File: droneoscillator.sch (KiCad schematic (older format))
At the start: 44 parts, among them J1 Conn_01x02, J2 Conn_01x03, Q1 BC337, Q2 BC337, Q3 BC337, Q4 BC337, U1 NE5532

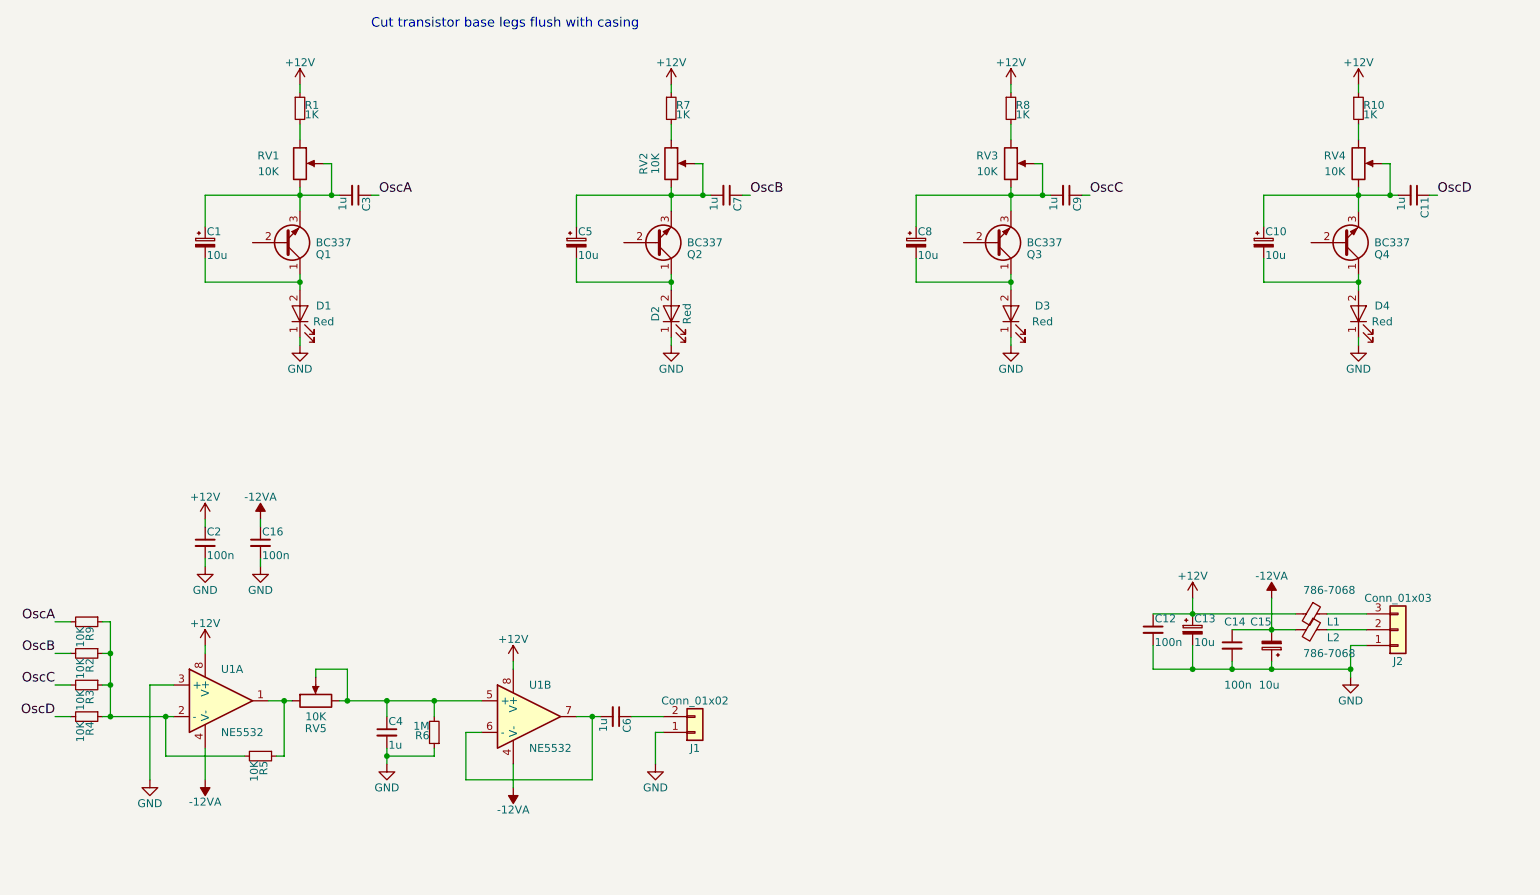
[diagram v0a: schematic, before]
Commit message: Bug fixes after first prototype build
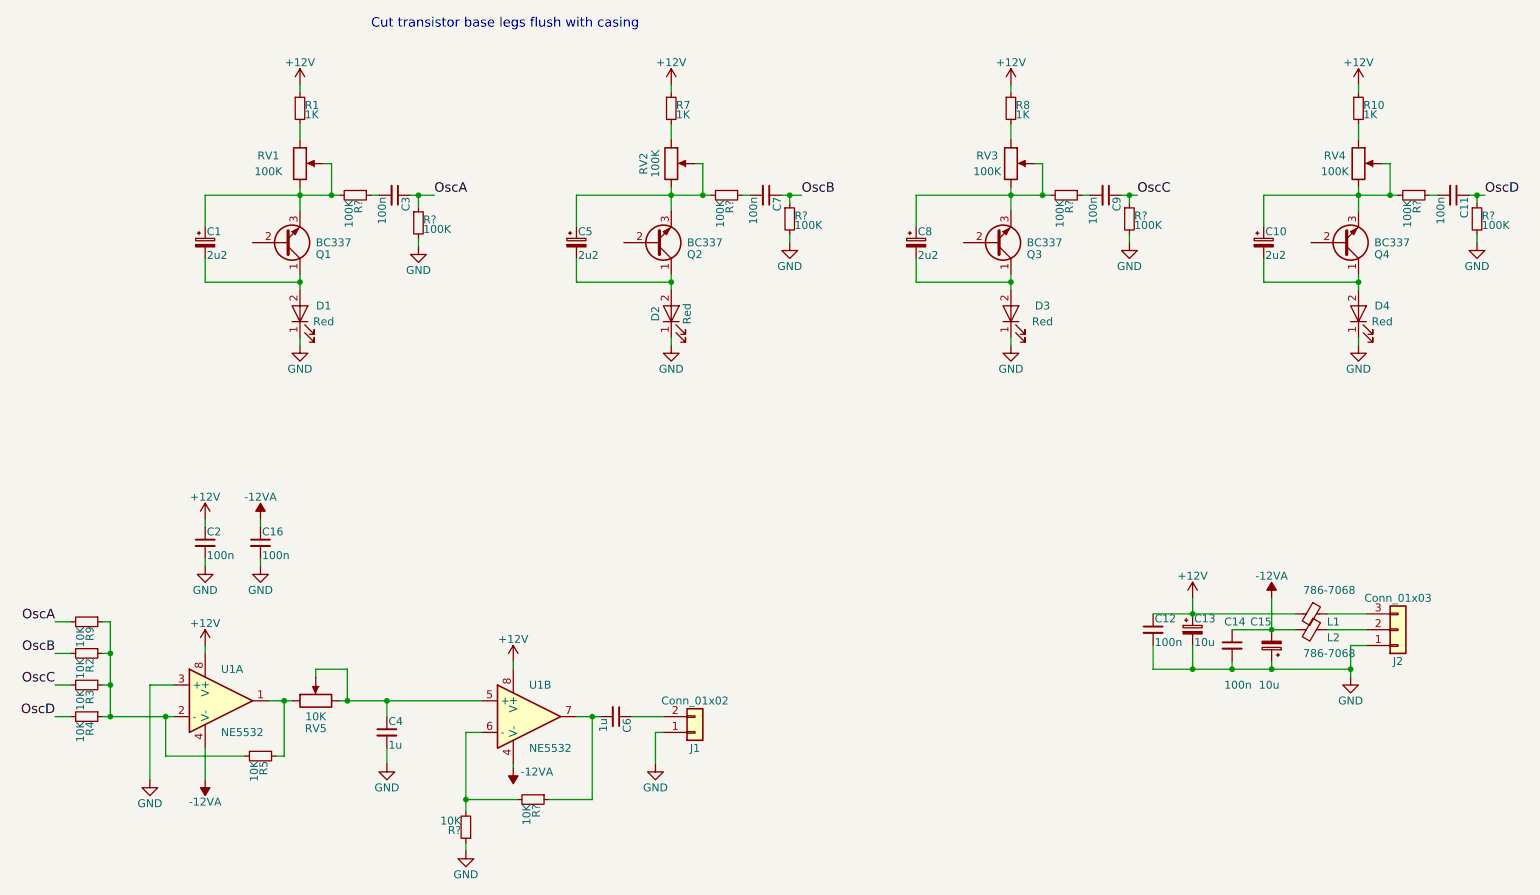
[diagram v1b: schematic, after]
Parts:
- removed R6: 1M, Resistors_THT:R_Axial_DIN0204_L3.6mm_D1.6mm_P7.62mm_Horizontal, symbol droneoscillator-rescue:R_Small
- added R? (x8): 100K, Resistors_THT:R_Axial_DIN0204_L3.6mm_D1.6mm_P7.62mm_Horizontal, symbol droneoscillator-rescue:R_Small
- added R? (x2): 10K, Resistors_THT:R_Axial_DIN0204_L3.6mm_D1.6mm_P7.62mm_Horizontal, symbol droneoscillator-rescue:R_Small
- C1, C10, C5, C8: value 10u -> 2u2
- C11, C3, C7, C9: value 1u -> 100n
- RV1, RV2, RV3, RV4: value 10K -> 100K
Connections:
- net GND: now also R?.1, R?.2, R?.2, R?.2, R?.2
- net OscA: now also R?.1
- net OscB: now also R?.1
- net OscC: now also R?.1
- net OscD: now also R?.1
- net at C1.1, Q1.3 (E), RV1.2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: now also R?.2; no longer C3.2
- net at C5.1, Q2.3 (E), RV2.2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: now also R?.2; no longer C7.2
- net at C8.1, Q3.3 (E), RV3.2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: now also R?.2; no longer C9.2
- net at C10.1, Q4.3 (E), RV4.2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: now also R?.2; no longer C11.2
- net at C6.2, U1.7: now also R?.1; no longer U1.6 (-)
- new net: R?.2, R?.2, U1.6 (-)
- new net: C3.2, R?.1
- new net: C7.2, R?.1
- new net: C9.2, R?.1
- new net: C11.2, R?.1
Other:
- moved on the sheet: C11, C3, C7, C9

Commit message: update after prototype build, new PCB layout
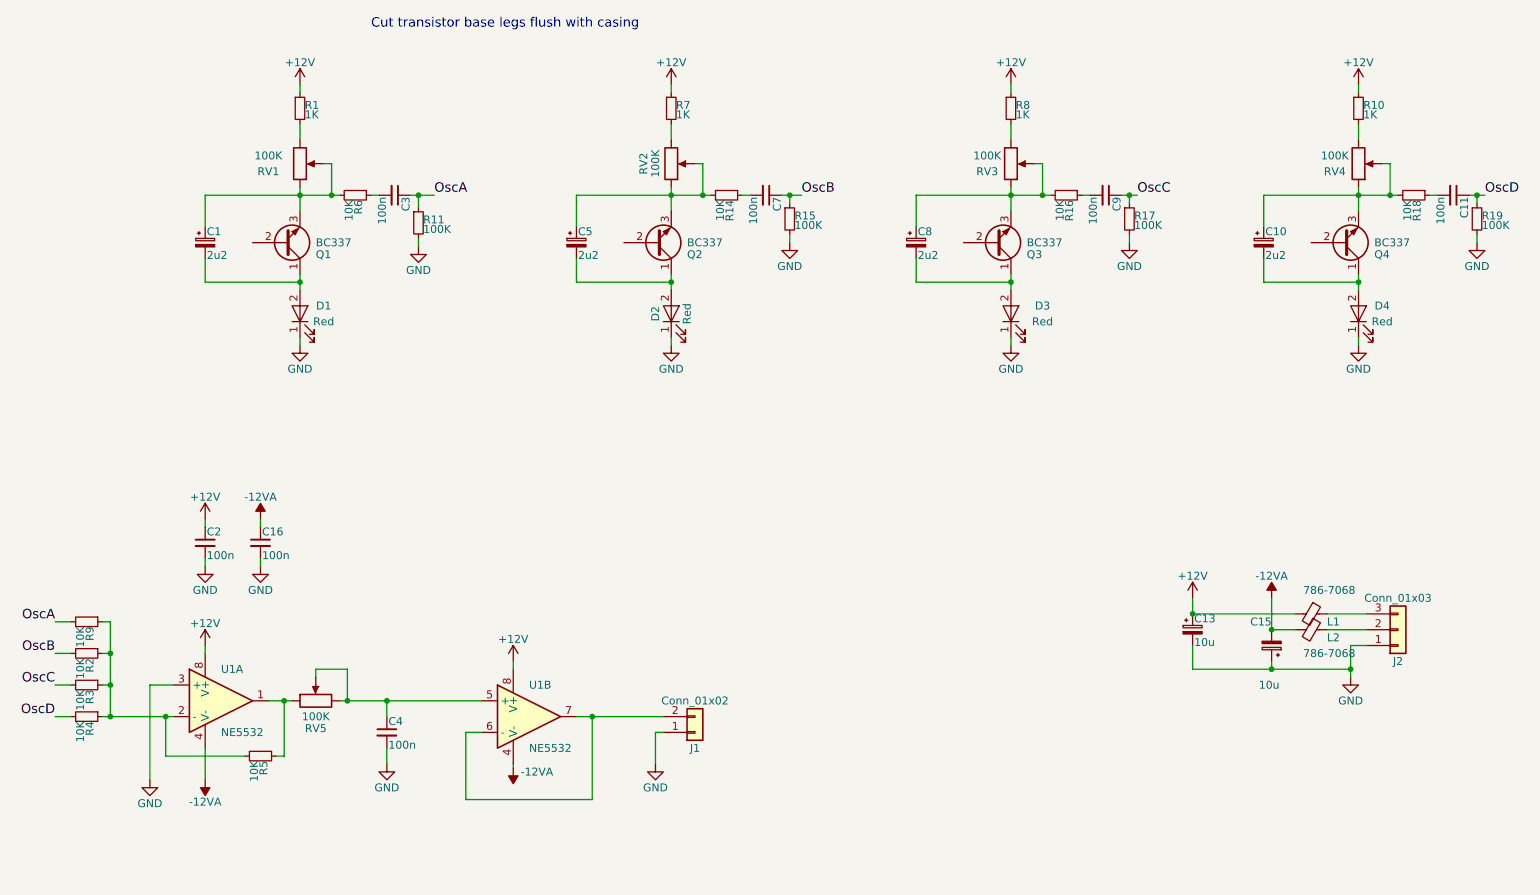
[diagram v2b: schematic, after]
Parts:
- removed C12, C14: 100n, Capacitors_THT:C_Disc_D4.3mm_W1.9mm_P5.00mm, symbol droneoscillator-rescue:C_Small
- removed C6: 1u, Capacitors_THT:C_Disc_D4.3mm_W1.9mm_P5.00mm, symbol droneoscillator-rescue:C_Small
- removed R? (x2): 10K, Resistors_THT:R_Axial_DIN0204_L3.6mm_D1.6mm_P7.62mm_Horizontal, symbol droneoscillator-rescue:R_Small
- C1, C10, C13, C15, C5, C8: footprint Capacitors_THT:CP_Radial_D5.0mm_P2.50mm -> Capacitor_THT:CP_Radial_D4.0mm_P2.00mm
- C11, C16, C2, C3, C7, C9: footprint Capacitors_THT:C_Disc_D4.3mm_W1.9mm_P5.00mm -> Capacitor_THT:C_Disc_D4.3mm_W1.9mm_P5.00mm
- C4: value 1u -> 100n; footprint Capacitors_THT:C_Disc_D4.3mm_W1.9mm_P5.00mm -> Capacitor_THT:C_Disc_D4.3mm_W1.9mm_P5.00mm
- J1: footprint Connectors_JST:JST_XH_B02B-XH-A_02x2.50mm_Straight -> Connector_JST:JST_XH_B02B-XH-A_1x02_P2.50mm_Vertical
- J2: footprint Connectors_JST:JST_XH_B03B-XH-A_03x2.50mm_Straight -> Connector_JST:JST_XH_B03B-XH-A_1x03_P2.50mm_Vertical
- L1, L2: footprint Inductors_SMD:L_0805_HandSoldering -> Inductor_SMD:L_0805_2012Metric
- Q1, Q2, Q3, Q4: footprint TO_SOT_Packages_THT:TO-92_Inline_Wide -> Package_TO_SOT_THT:TO-92_Inline_Wide
- R1, R10, R2, R3, R4, R5, R7, R8, R9: footprint Resistors_THT:R_Axial_DIN0204_L3.6mm_D1.6mm_P7.62mm_Horizontal -> Resistor_THT:R_Axial_DIN0204_L3.6mm_D1.6mm_P7.62mm_Horizontal
- R11, R15, R17, R19: renamed from R?; footprint Resistors_THT:R_Axial_DIN0204_L3.6mm_D1.6mm_P7.62mm_Horizontal -> Resistor_THT:R_Axial_DIN0204_L3.6mm_D1.6mm_P7.62mm_Horizontal
- R14, R16, R18, R6: renamed from R?; value 100K -> 10K; footprint Resistors_THT:R_Axial_DIN0204_L3.6mm_D1.6mm_P7.62mm_Horizontal -> Resistor_THT:R_Axial_DIN0204_L3.6mm_D1.6mm_P7.62mm_Horizontal
- RV5: value 10K -> 100K
- U1: footprint Housings_DIP:DIP-8_W7.62mm_LongPads -> Package_DIP:DIP-8_W7.62mm_Socket_LongPads
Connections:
- net at C1.1, Q1.3 (E), R6.2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: now also RV1.1; no longer RV1.3
- net at R1.2: now also RV1.3; no longer RV1.1
- net at C5.1, Q2.3 (E), R14.2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: now also RV2.1; no longer RV2.3
- net at R7.2: now also RV2.3; no longer RV2.1
- net at RV3.1: now also C8.1, Q3.3 (E), R16.2, RV3.2; no longer R8.2
- net at RV4.1: now also C10.1, Q4.3 (E), R18.2, RV4.2; no longer R10.2
- net at U1.6 (-): now also J1.2 (Pin_2), U1.7
- new net: R8.2, RV3.3
- new net: R10.2, RV4.3

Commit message: schematic bugfix, minor changes to PCB
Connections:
- net at R5.1, U1.1: now also RV5.3; no longer RV5.1
- net at C4.1, RV5.2, U1.5 (+): now also RV5.1; no longer RV5.3
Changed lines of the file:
@@
 F 3 "" H 2850 5150 50  0001 C CNN
 	1    2850 5150
-	0    -1   -1   0
+	0    1    -1   0
 $EndComp
 $Comp

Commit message: silkscreen bugfix
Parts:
- D1, D2, D3, D4: footprint LEDs:LED_D5.0mm_Horizontal_O1.27mm_Z3.0mm -> LED_THT:LED_D5.0mm_Horizontal_O1.27mm_Z3.0mm
- RV1, RV2, RV3, RV4, RV5: footprint Potentiometers:Potentiometer_Alps_RK097_Single_Vertical -> Potentiometer_THT:Potentiometer_Alps_RK097_Single_Horizontal
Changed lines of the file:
@@
 F 0 "RV1" H 2550 1800 50  0000 C CNN
 F 1 "100K" H 2550 1700 50  0000 C CNN
-F 2 "Potentiometers:Potentiometer_Alps_RK097_Single_Vertical" H 2750 1750 50  0001 C CNN
+F 2 "Potentiometer_THT:Potentiometer_Alps_RK097_Single_Horizontal" H 2750 1750 50  0001 C CNN
 F 3 "" H 2750 1750 50  0001 C CNN
 	1    2750 1750
@@
 F 0 "D1" V 2800 2550 50  0000 C CNN
 F 1 "Red" V 2700 2550 50  0000 C CNN
-F 2 "LEDs:LED_D5.0mm_Horizontal_O1.27mm_Z3.0mm" H 2750 2700 50  0001 C CNN
+F 2 "LED_THT:LED_D5.0mm_Horizontal_O1.27mm_Z3.0mm" H 2750 2700 50  0001 C CNN
 F 3 "" H 2750 2700 50  0001 C CNN
 	1    2750 2700
@@
 F 0 "RV3" H 7100 1800 50  0000 C CNN
 F 1 "100K" H 7100 1700 50  0000 C CNN
-F 2 "Potentiometers:Potentiometer_Alps_RK097_Single_Vertical" H 7250 1750 50  0001 C CNN
+F 2 "Potentiometer_THT:Potentiometer_Alps_RK097_Single_Horizontal" H 7250 1750 50  0001 C CNN
 F 3 "" H 7250 1750 50  0001 C CNN
 	1    7250 1750
@@
 F 0 "D2" H 5100 2800 50  0000 C CNN
 F 1 "Red" H 5100 2600 50  0000 C CNN
-F 2 "LEDs:LED_D5.0mm_Horizontal_O1.27mm_Z3.0mm" H 5100 2700 50  0001 C CNN
+F 2 "LED_THT:LED_D5.0mm_Horizontal_O1.27mm_Z3.0mm" H 5100 2700 50  0001 C CNN
 F 3 "" H 5100 2700 50  0001 C CNN
 	1    5100 2700
@@
 F 0 "RV4" H 9300 1800 50  0000 C CNN
 F 1 "100K" H 9300 1700 50  0000 C CNN
-F 2 "Potentiometers:Potentiometer_Alps_RK097_Single_Vertical" H 9450 1750 50  0001 C CNN
+F 2 "Potentiometer_THT:Potentiometer_Alps_RK097_Single_Horizontal" H 9450 1750 50  0001 C CNN
 F 3 "" H 9450 1750 50  0001 C CNN
 	1    9450 1750
@@
 F 0 "D3" V 7300 2500 50  0000 C CNN
 F 1 "Red" V 7200 2500 50  0000 C CNN
-F 2 "LEDs:LED_D5.0mm_Horizontal_O1.27mm_Z3.0mm" H 7250 2700 50  0001 C CNN
+F 2 "LED_THT:LED_D5.0mm_Horizontal_O1.27mm_Z3.0mm" H 7250 2700 50  0001 C CNN
 F 3 "" H 7250 2700 50  0001 C CNN
 	1    7250 2700
@@
 F 0 "RV2" V 4925 1750 50  0000 C CNN
 F 1 "100K" V 5000 1750 50  0000 C CNN
-F 2 "Potentiometers:Potentiometer_Alps_RK097_Single_Vertical" H 5100 1750 50  0001 C CNN
+F 2 "Potentiometer_THT:Potentiometer_Alps_RK097_Single_Horizontal" H 5100 1750 50  0001 C CNN
 F 3 "" H 5100 1750 50  0001 C CNN
 	1    5100 1750
@@
 F 0 "RV5" V 2675 5150 50  0000 C CNN
 F 1 "100K" V 2750 5150 50  0000 C CNN
-F 2 "Potentiometers:Potentiometer_Alps_RK097_Single_Vertical" H 2850 5150 50  0001 C CNN
+F 2 "Potentiometer_THT:Potentiometer_Alps_RK097_Single_Horizontal" H 2850 5150 50  0001 C CNN
 F 3 "" H 2850 5150 50  0001 C CNN
 	1    2850 5150
@@
 F 0 "D4" V 9500 2550 50  0000 C CNN
 F 1 "Red" V 9400 2550 50  0000 C CNN
-F 2 "LEDs:LED_D5.0mm_Horizontal_O1.27mm_Z3.0mm" H 9450 2700 50  0001 C CNN
+F 2 "LED_THT:LED_D5.0mm_Horizontal_O1.27mm_Z3.0mm" H 9450 2700 50  0001 C CNN
 F 3 "" H 9450 2700 50  0001 C CNN
 	1    9450 2700
